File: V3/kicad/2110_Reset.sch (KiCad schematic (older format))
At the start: 7 parts, among them SW1000 SW_Push, U1000 LM555xM

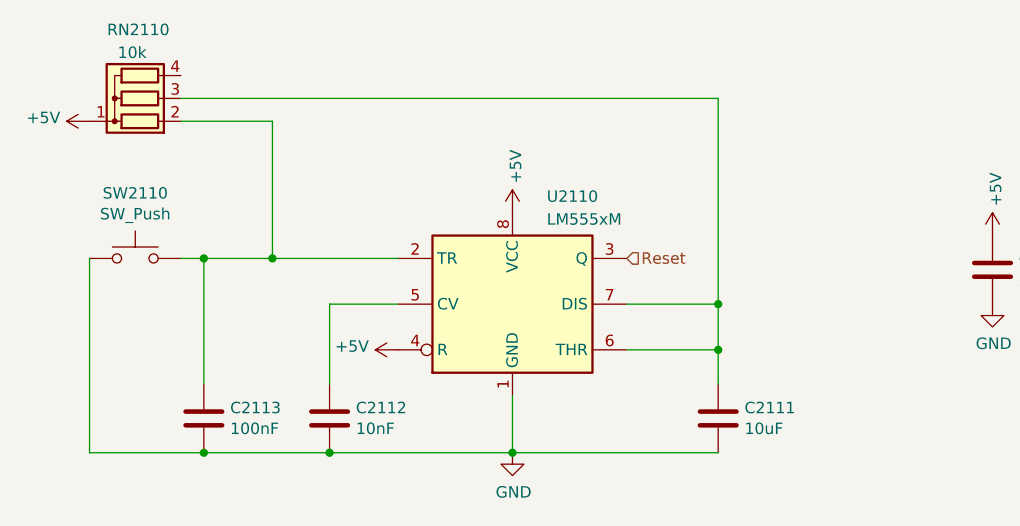
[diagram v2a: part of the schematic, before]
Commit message: 3 1 1 m memory (#15)
* moved EEPROM files to /old

* Reworking 3.0 board

* changed footprint on RAM chip

* cleared out old memory traces

* started on rerouting

* on to autoroute

* little more cleanup

* more cleanup

* ill let the autoroute do the rest

* reroute complete

* made PQFP leads fatter

* Updated GAL logic

* Design Rule Check

* Minor pcb touch up

* gerber files

* just totally redid the whole thing

* More rearranging

* added a few caps

* Routed ROM and RAM together

* more routing

* more routes

* A lot of disorganized changes

* 3.1 CSIO SPI Bus (#9)

* Updated SPI to use CPU signals

8 bit register chip controls CS lines

* Renamed and added caps to SD page

* Cleanup

* 3.1 Resistor Replacement (#10)

* First two R arrays

* Added one more r array

* added cap for SPI FF

* Extended cpu pads (#12)

* 3.1 fix sheet hierarchy (#13)

* Fixed Schematic Heirarchy issue

* some footprints re-added to board

* Add footprints added

* Minor changes

* 3.1 redraw cpu courtyard (#14)

* moved all crtyd lines to same place in file

* Duplicate lines were causing issues

* Added pin header for SPI lines

* routed last of non-bus lines

* attempted to route memory lines

* Added new symbol and footprint

* CTS0 no longer drives an LED

* Final cleanup before memory routing

* got CTS0 and RTS mixed up

* Removed extra led from board

* Updated signature

* small changes
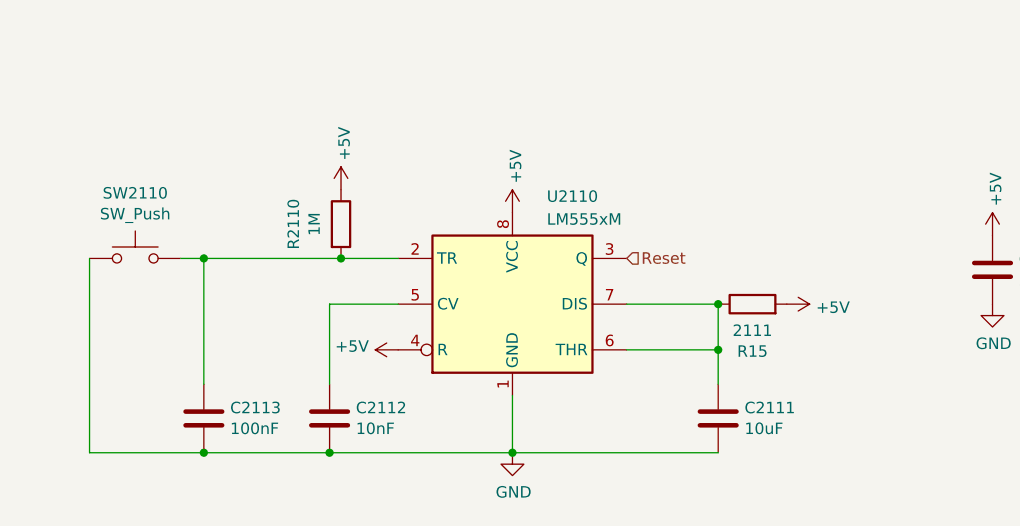
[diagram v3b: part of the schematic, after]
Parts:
- removed RN2110: 10k, Resistor_THT:R_Array_SIP4, symbol Device:R_Network03
- added R14: 1M, Resistor_SMD:R_1206_3216Metric, symbol Device:R
- added R15: 2111, Resistor_SMD:R_1206_3216Metric, symbol Device:R
- C1000, C1001, C1002, C1003: footprint Capacitor_THT:C_Rect_L4.0mm_W2.5mm_P2.50mm -> Capacitor_SMD:C_1206_3216Metric
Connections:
- net +5V: now also R14.1, R15.2
- net at C1003.1, SW1000.2, U1000.2 (TR): now also R14.2
- net at C1002.1, U1000.6 (THR), U1000.7 (DIS): now also R15.1
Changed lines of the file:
@@
 $Descr A4 11693 8268
 encoding utf-8
-Sheet 8 9
+Sheet 4 6
 Title ""
 Date ""
@@
 AR Path="/6191B6A2/624CF3AF/624C743E" Ref="U?"  Part="1"
 AR Path="/6191B6A2/61EBDADB/62512FB8/624C743E" Ref="U2110"  Part="1"
+AR Path="/63A83936/62512FB8/624C743E" Ref="U2110"  Part="1"
 F 0 "U2110" H 5950 4550 50  0000 L TNN
 F 1 "LM555xM" H 5950 4450 50  0000 L TNN
@@
 AR Path="/6191B6A2/624CF3AF/624C7444" Ref="#PWR?"  Part="1"
 AR Path="/6191B6A2/61EBDADB/62512FB8/624C7444" Ref="#PWR0105"  Part="1"
+AR Path="/63A83936/62512FB8/624C7444" Ref="#PWR0105"  Part="1"
 F 0 "#PWR0105" H 5800 4450 50  0001 C CNN
 F 1 "GND" H 5805 4527 50  0000 C CNN
@@
 AR Path="/6191B6A2/624CF3AF/624C744A" Ref="SW?"  Part="1"
 AR Path="/6191B6A2/61EBDADB/62512FB8/624C744A" Ref="SW2110"  Part="1"
+AR Path="/63A83936/62512FB8/624C744A" Ref="SW2110"  Part="1"
 F 0 "SW2110" H 4150 4135 50  0000 C CNN
 F 1 "SW_Push" H 4150 4044 50  0000 C CNN
@@
 AR Path="/6191B6A2/624CF3AF/624C7456" Ref="C?"  Part="1"
 AR Path="/6191B6A2/61EBDADB/62512FB8/624C7456" Ref="C2112"  Part="1"
+AR Path="/63A83936/62512FB8/624C7456" Ref="C2112"  Part="1"
 F 0 "C2112" H 5115 4596 50  0000 L CNN
 F 1 "10nF" H 5115 4505 50  0000 L CNN
-F 2 "Capacitor_THT:C_Rect_L4.0mm_W2.5mm_P2.50mm" H 5038 4400 50  0001 C CNN
+F 2 "Capacitor_SMD:C_1206_3216Metric" H 5038 4400 50  0001 C CNN
 F 3 "~" H 5000 4550 50  0001 C CNN
 	1    5000 4550
@@
 Wire Wire Line
 	6700 4250 6700 4050
-Connection ~ 6700 4050
 $Comp
 L Device:C C?
@@
 AR Path="/6191B6A2/624CF3AF/624C7467" Ref="C?"  Part="1"
 AR Path="/6191B6A2/61EBDADB/62512FB8/624C7467" Ref="C2111"  Part="1"
+AR Path="/63A83936/62512FB8/624C7467" Ref="C2111"  Part="1"
 F 0 "C2111" H 6815 4596 50  0000 L CNN
 F 1 "10uF" H 6815 4505 50  0000 L CNN
-F 2 "Capacitor_THT:C_Rect_L4.0mm_W2.5mm_P2.50mm" H 6738 4400 50  0001 C CNN
+F 2 "Capacitor_SMD:C_1206_3216Metric" H 6738 4400 50  0001 C CNN
 F 3 "~" H 6700 4550 50  0001 C CNN
 	1    6700 4550
@@
 AR Path="/6191B6A2/624CF3AF/625B99BC" Ref="C?"  Part="1"
 AR Path="/6191B6A2/61EBDADB/62512FB8/625B99BC" Ref="C2110"  Part="1"
+AR Path="/63A83936/62512FB8/625B99BC" Ref="C2110"  Part="1"
 F 0 "C2110" H 8015 3946 50  0000 L CNN
 F 1 "22pF" H 8015 3855 50  0000 L CNN
-F 2 "Capacitor_THT:C_Rect_L4.0mm_W2.5mm_P2.50mm" H 7938 3750 50  0001 C CNN
+F 2 "Capacitor_SMD:C_1206_3216Metric" H 7938 3750 50  0001 C CNN
 F 3 "~" H 7900 3900 50  0001 C CNN
 	1    7900 3900
@@
 AR Path="/6191B6A2/624CF3AF/625BC077" Ref="#PWR?"  Part="1"
 AR Path="/6191B6A2/61EBDADB/62512FB8/625BC077" Ref="#PWR0106"  Part="1"
+AR Path="/63A83936/62512FB8/625BC077" Ref="#PWR0106"  Part="1"
 F 0 "#PWR0106" H 7900 3800 50  0001 C CNN
 F 1 "GND" H 7905 3877 50  0000 C CNN
@@
 AR Path="/6191B6A2/624CF3AF/62633FFA" Ref="C?"  Part="1"
 AR Path="/6191B6A2/61EBDADB/62512FB8/62633FFA" Ref="C2113"  Part="1"
+AR Path="/63A83936/62512FB8/62633FFA" Ref="C2113"  Part="1"
 F 0 "C2113" H 4565 4596 50  0000 L CNN
 F 1 "100nF" H 4565 4505 50  0000 L CNN
-F 2 "Capacitor_THT:C_Rect_L4.0mm_W2.5mm_P2.50mm" H 4488 4400 50  0001 C CNN
+F 2 "Capacitor_SMD:C_1206_3216Metric" H 4488 4400 50  0001 C CNN
 F 3 "~" H 4450 4550 50  0001 C CNN
 	1    4450 4550
@@
 Wire Wire Line
 	4450 4400 4450 3850
-Connection ~ 4750 3850
 Text Notes 7850 6900 0    118  ~ 24
 This page has been checked!
-$Comp
-L power:+5V #PWR0103
-U 1 1 61E872A1
-P 3950 3250
-AR Path="/61D852D7/61E872A1" Ref="#PWR0103"  Part="1"
-AR Path="/6191B6A2/624CF3AF/61E872A1" Ref="#PWR?"  Part="1"
-AR Path="/6191B6A2/61EBDADB/62512FB8/61E872A1" Ref="#PWR0108"  Part="1"
-F 0 "#PWR0108" H 3950 3100 50  0001 C CNN
-F 1 "+5V" V 3965 3378 50  0000 L CNN
-F 2 "" H 3950 3250 50  0001 C CNN
-F 3 "" H 3950 3250 50  0001 C CNN
-	1    3950 3250
-	0    -1   -1   0
-$EndComp
 $Comp
 L power:+5V #PWR0104
@@
 AR Path="/6191B6A2/624CF3AF/61E87BC4" Ref="#PWR?"  Part="1"
 AR Path="/6191B6A2/61EBDADB/62512FB8/61E87BC4" Ref="#PWR0109"  Part="1"
+AR Path="/63A83936/62512FB8/61E87BC4" Ref="#PWR0109"  Part="1"
 F 0 "#PWR0109" H 5800 3500 50  0001 C CNN
 F 1 "+5V" V 5815 3778 50  0000 L CNN
@@
 AR Path="/6191B6A2/624CF3AF/61E8CD41" Ref="#PWR?"  Part="1"
 AR Path="/6191B6A2/61EBDADB/62512FB8/61E8CD41" Ref="#PWR0115"  Part="1"
+AR Path="/63A83936/62512FB8/61E8CD41" Ref="#PWR0115"  Part="1"
 F 0 "#PWR0115" H 7900 3600 50  0001 C CNN
 F 1 "+5V" V 7915 3878 50  0000 L CNN
@@
 AR Path="/6191B6A2/624CF3AF/620357A9" Ref="#PWR?"  Part="1"
 AR Path="/6191B6A2/61EBDADB/62512FB8/620357A9" Ref="#PWR0121"  Part="1"
+AR Path="/63A83936/62512FB8/620357A9" Ref="#PWR0121"  Part="1"
 F 0 "#PWR0121" H 5300 4100 50  0001 C CNN
 F 1 "+5V" V 5315 4378 50  0000 L CNN
@@
 Connection ~ 4450 4700
 Wire Wire Line
-	4450 3850 4750 3850
-Wire Wire Line
 	4450 4700 5000 4700
-Wire Wire Line
-	4750 3850 5300 3850
-$Comp
-L Device:R_Network03 RN2110
-U 1 1 6256C4FE
-P 4150 3150
-F 0 "RN2110" V 4450 3000 50  0000 L CNN
-F 1 "10k" V 4350 3100 50  0000 L CNN
-F 2 "Resistor_THT:R_Array_SIP4" V 4425 3150 50  0001 C CNN
-F 3 "http://www.vishay.com/docs/31509/csc.pdf" H 4150 3150 50  0001 C CNN
-	1    4150 3150
+$Comp
+L power:+5V #PWR?
+U 1 1 62F79AB5
+P 7000 4050
+AR Path="/6191B6A2/61EBDADB/62F79AB5" Ref="#PWR?"  Part="1"
+AR Path="/6191B6A2/61EBDADB/62512FB8/62F79AB5" Ref="#PWR0108"  Part="1"
+AR Path="/63A83936/62512FB8/62F79AB5" Ref="#PWR0108"  Part="1"
+F 0 "#PWR0108" H 7000 3900 50  0001 C CNN
+F 1 "+5V" V 7015 4178 50  0000 L CNN
+F 2 "" H 7000 4050 50  0001 C CNN
+F 3 "" H 7000 4050 50  0001 C CNN
+	1    7000 4050
+	0    1    1    0
+$EndComp
+$Comp
+L Device:R R?
+U 1 1 62F79ABB
+P 5050 3700
+AR Path="/6191B6A2/61EBDADB/62F79ABB" Ref="R?"  Part="1"
+AR Path="/6191B6A2/61EBDADB/62512FB8/62F79ABB" Ref="R14"  Part="1"
+AR Path="/63A83936/62512FB8/62F79ABB" Ref="R2110"  Part="1"
+F 0 "R2110" V 4843 3700 50  0000 C CNN
+F 1 "1M" V 4934 3700 50  0000 C CNN
+F 2 "Resistor_SMD:R_1206_3216Metric" V 4980 3700 50  0001 C CNN
+F 3 "~" H 5050 3700 50  0001 C CNN
+	1    5050 3700
+	1    0    0    -1
+$EndComp
+$Comp
+L power:+5V #PWR?
+U 1 1 62F79AC1
+P 5050 3550
+AR Path="/6191B6A2/61EBDADB/62F79AC1" Ref="#PWR?"  Part="1"
+AR Path="/6191B6A2/61EBDADB/62512FB8/62F79AC1" Ref="#PWR0155"  Part="1"
+AR Path="/63A83936/62512FB8/62F79AC1" Ref="#PWR0155"  Part="1"
+F 0 "#PWR0155" H 5050 3400 50  0001 C CNN
+F 1 "+5V" V 5065 3678 50  0000 L CNN
+F 2 "" H 5050 3550 50  0001 C CNN
+F 3 "" H 5050 3550 50  0001 C CNN
+	1    5050 3550
+	1    0    0    -1
+$EndComp
+Connection ~ 5050 3850
+Wire Wire Line
+	5050 3850 5300 3850
+Wire Wire Line
+	4450 3850 5050 3850
+$Comp
+L Device:R R?
+U 1 1 62F79AAF
+P 6850 4050
+AR Path="/6191B6A2/61EBDADB/62F79AAF" Ref="R?"  Part="1"
+AR Path="/6191B6A2/61EBDADB/62512FB8/62F79AAF" Ref="R15"  Part="1"
+AR Path="/63A83936/62512FB8/62F79AAF" Ref="R15"  Part="1"
+F 0 "R15" V 6643 4050 50  0000 C CNN
+F 1 "2111" V 6734 4050 50  0000 C CNN
+F 2 "Resistor_SMD:R_1206_3216Metric" V 6780 4050 50  0001 C CNN
+F 3 "~" H 6850 4050 50  0001 C CNN
+	1    6850 4050
 	0    -1   -1   0
 $EndComp
-Wire Wire Line
-	4350 3250 4750 3250
-Wire Wire Line
-	4750 3250 4750 3850
-Wire Wire Line
-	4350 3150 6700 3150
-Wire Wire Line
-	6700 3150 6700 4050
+Connection ~ 6700 4050
 $EndSCHEMATC

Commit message: new board layout, not routing yet, still need to check schematics
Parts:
- U1000: footprint Package_SO:SOIC-8_3.9x4.9mm_P1.27mm -> Package_DIP:DIP-8_W7.62mm_LongPads
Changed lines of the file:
@@
 F 0 "U2110" H 5950 4550 50  0000 L TNN
 F 1 "LM555xM" H 5950 4450 50  0000 L TNN
-F 2 "Package_SO:SOIC-8_3.9x4.9mm_P1.27mm" H 6650 3650 50  0001 C CNN
+F 2 "Package_DIP:DIP-8_W7.62mm_LongPads" H 6650 3650 50  0001 C CNN
 F 3 "http://www.ti.com/lit/ds/symlink/lm555.pdf" H 6650 3650 50  0001 C CNN
 	1    5800 4050
